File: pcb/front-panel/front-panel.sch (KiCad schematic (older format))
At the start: 26 parts, among them J1 HEADER-1x06, J2 HEADER-1x01, J3 HEADER-1x01, J4 HEADER-1x01, J5 HEADER-1x01, U1 ER-OLED1602-4W, U2 LT1109CS8-12

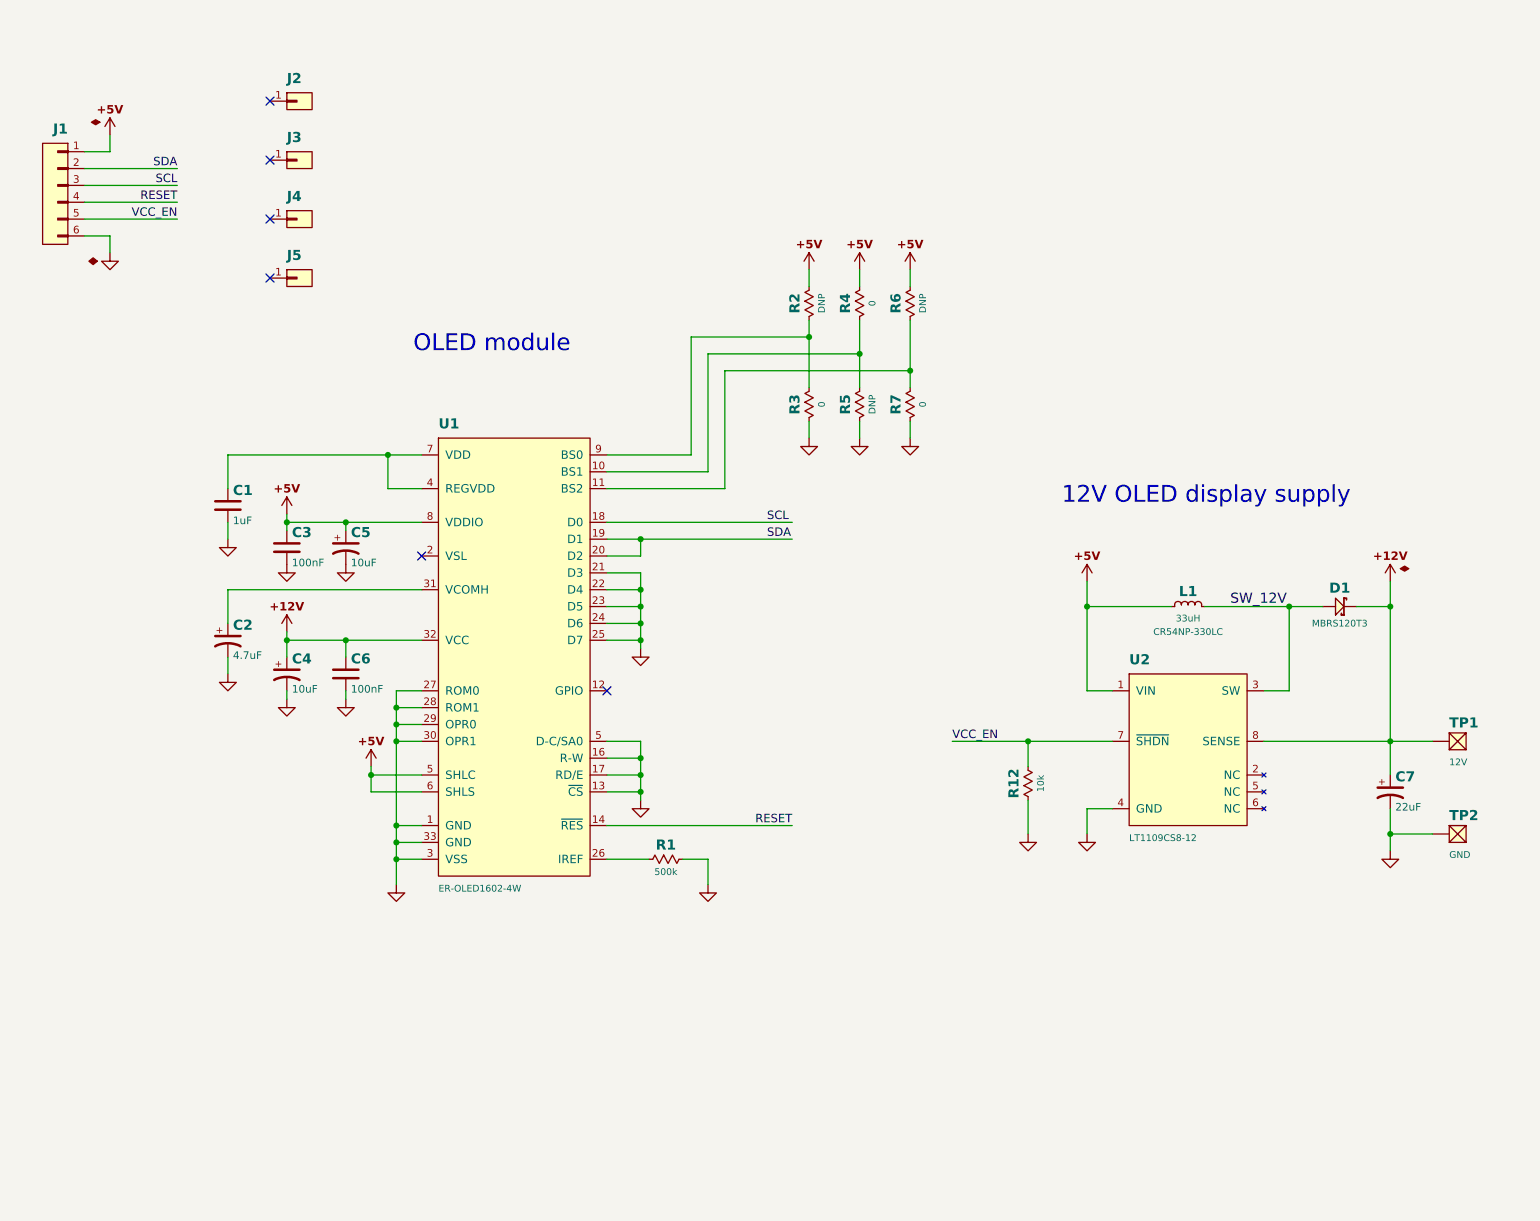
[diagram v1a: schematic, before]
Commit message: Added pull down resistor to Reset line.
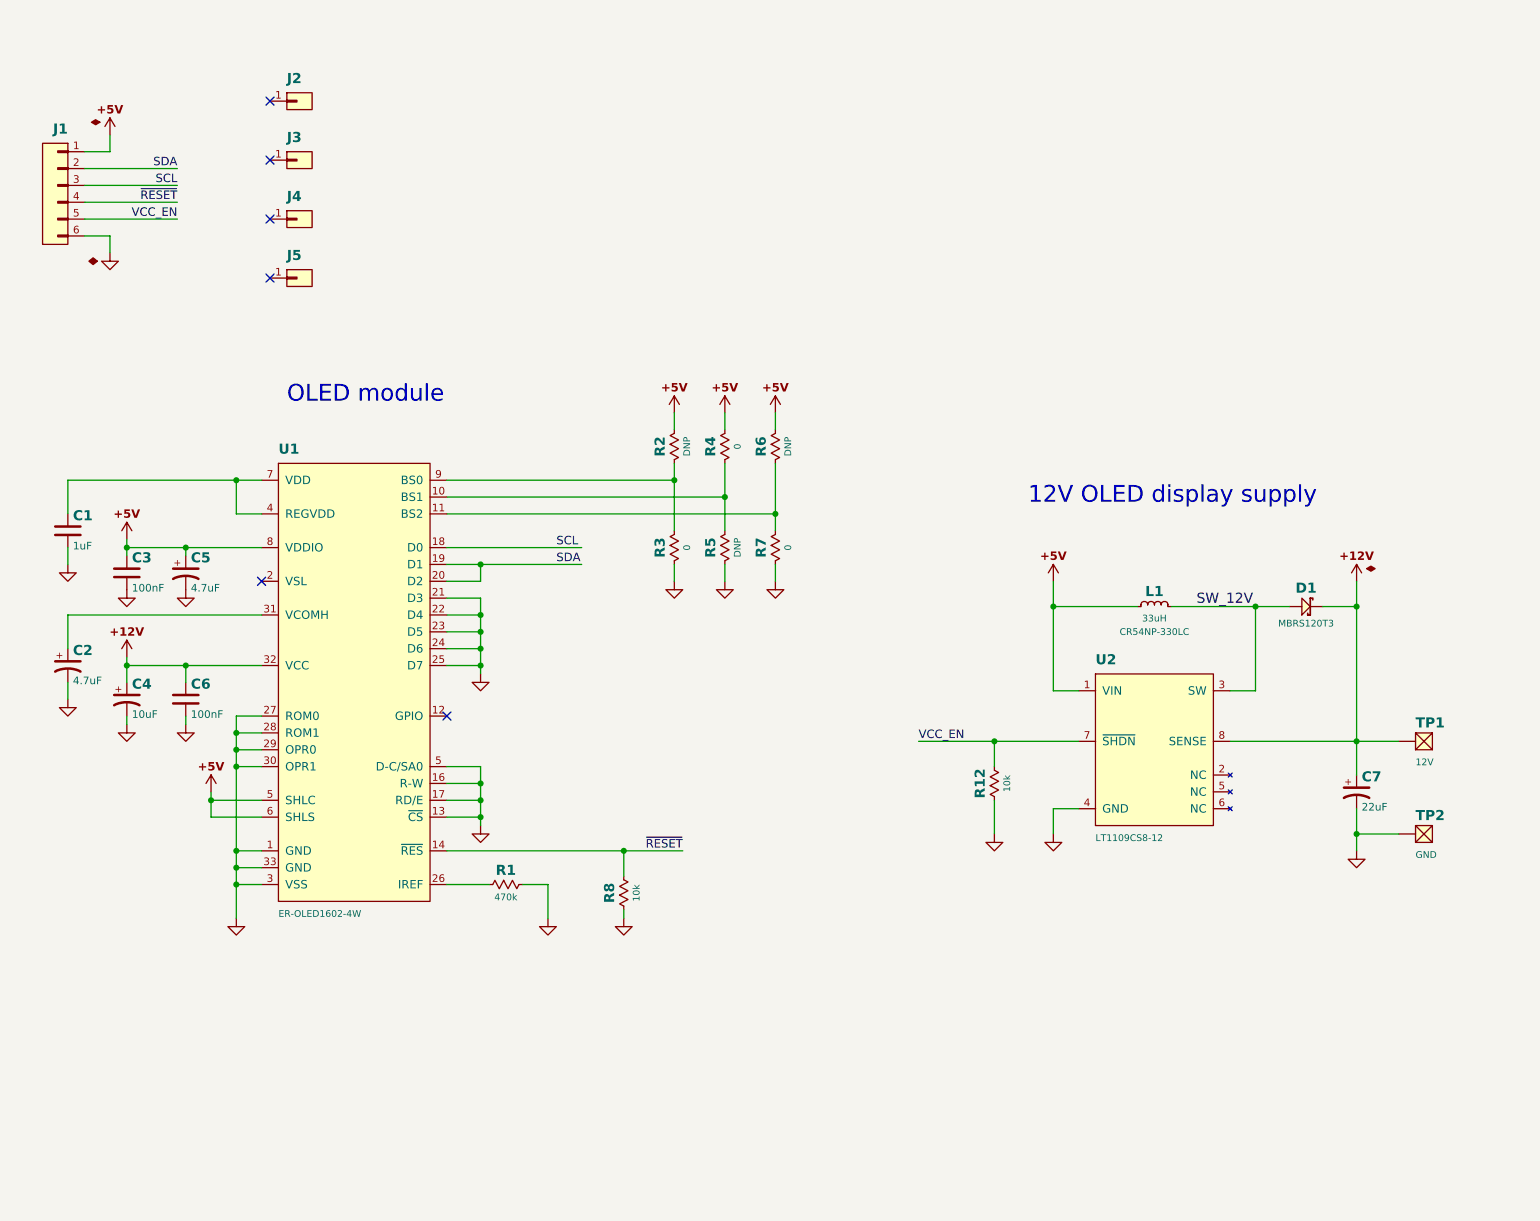
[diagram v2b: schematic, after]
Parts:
- added R8: 10k, SMT:R-0603, symbol RESISTOR
- C5: value 10uF -> 4.7uF
- R1: value 500k -> 470k
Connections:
- net GND: now also R8.1
- net RESET renamed ~RESET
- net ~RESET: now also R8.2
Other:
- moved on the sheet: C1, C2, C3, C4, C5, C6, C7, D1, L1, R1, R12, R2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

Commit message: Revised touch and front panel PCB, Added Motherboard PCB
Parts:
- removed R12: 10k, SMT:R-0603, symbol RESISTOR
- removed R2, R5, R6: DNP, SMT:R-0603, symbol RESISTOR
- removed R3, R4, R7: 0, SMT:R-0603, symbol RESISTOR
- added C10: 3.3uF, smt:C-0805, symbol passive:CAP
- added C8: 100nF, smt:C-0603, symbol passive:CAP
- added C9: 1uF, smt:C-0805, symbol passive:CAP
- added J6: HEADER-1x01, conn-wire-pads:SolderPad-100x300, symbol connectors:HEADER-1x01
- added Q1, Q2: BSS138, smt-sot:SOT23, symbol passive:N-MOSFET
- added R2: 10k, smt:R-0603, symbol passive:RESISTOR
- added R4, R5: 4.7k, smt:R-0603, symbol passive:RESISTOR
- added TP3: 3.3V, conn-wire-pads:TEST-POINT-50, symbol connectors:TEST-POINT
- added U3: TSL2591, smt-dfn:DFN6, symbol ic-misc:TSL2591
- added U4: LP2981-33DBVT, smt-sot:SOT23-5, symbol ic-power:LP2981
- C1: footprint SMT:C-0805 -> smt:C-0805; symbol CAP -> passive:CAP
- C2: footprint SMT:CPL-1206 -> smt:CPL-1206; symbol CAP-E -> passive:CAP-E
- C3, C6: footprint SMT:C-0603 -> smt:C-0603; symbol CAP -> passive:CAP
- C4, C5: footprint SMT:CPL-0805 -> smt:CPL-0805; symbol CAP-E -> passive:CAP-E
- C7: footprint SMT:CPL-2312 -> smt:CPL-2312; symbol CAP-E -> passive:CAP-E
- D1: footprint SMT:DO-214-AA -> smt:DO-214-AA; symbol SCHOTTKY -> passive:SCHOTTKY
- J1: footprint Conn-Wire-Pads:WP-50mil-1x06 -> conn-wire-pads:WP-50mil-1x06; symbol HEADER-1x06 -> connectors:HEADER-1x06
- J2, J3, J4: footprint Conn-Wire-Pads:SolderPad-100x500 -> conn-wire-pads:SolderPad-100x500; symbol HEADER-1x01 -> connectors:HEADER-1x01
- J5: footprint Conn-Wire-Pads:SolderPad-100x150 -> conn-wire-pads:SolderPad-100x300; symbol HEADER-1x01 -> connectors:HEADER-1x01
- L1: footprint SMT:IND-CD54 -> smt:IND-CD54; symbol INDUCTOR -> passive:INDUCTOR
- R1: value 470k -> 500k; footprint SMT:R-0603 -> smt:R-0603; symbol RESISTOR -> passive:RESISTOR
- R8: footprint SMT:R-0603 -> smt:R-0603; symbol RESISTOR -> passive:RESISTOR
- TP1, TP2: footprint Conn-Wire-Pads:TEST-POINT-50 -> conn-wire-pads:TEST-POINT-50; symbol TEST-POINT -> connectors:TEST-POINT
- U1: footprint Misc:LCD-ER-OLED1602 -> misc:LCD-ER-OLED1602; symbol ER-OLED1602-4W -> opto:ER-OLED1602-4W
- U2: footprint SMT-SOIC:SOIC8 -> smt-soic:SOIC8; symbol LT1109CS8 -> ic-power:LT1109CS8
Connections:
- net labels added: +3V3, INT, SCL_3V3, SDA_3V3
- net labels removed: VCC_EN
- wire segments 86 -> 142
- no-connect marks 6 -> 8
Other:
- note added: "3.3V Regulator"
- note added: "I2C ADDR : 0x29"
- note added: "I2C ADDR : 0x78"
- note added: "I2C level shifter"
- note added: "Light sensor"
- moved on the sheet: C1, C2, C3, C4, C5, C6, C7, D1, L1, R1, R8, TP1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

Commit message: Updated PCB design
+ Completed daughterboard PCB layout.
* Corrected soldermask clerance on front panel pcb.
- Removed input resistor on DIN for RGB lamp board.
* Modified PCB layout for PSU board.
* Updated gerber files.
* Updated schematics pdf, BOM.
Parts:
- H5: renamed from J6; footprint conn-wire-pads:SolderPad-100x300 -> conn-wire-pads:SolderPad-100x200
- Q1, Q2: symbol passive:N-MOSFET -> transistor:N-MOSFET
- renumbered J2 to H1, J3 to H2, J4 to H3, J5 to H4, R8 to R3
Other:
- note added: "I2C Addr. : 0x29"
- note added: "I2C Addr. : 0x78"
- note removed: "I2C ADDR : 0x29"
- note removed: "I2C ADDR : 0x78"
- moved on the sheet: C1, C2, C3, C4, C5, C6, H1, H2, H3, H4, H5, J1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
